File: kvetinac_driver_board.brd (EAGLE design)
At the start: 73.7 x 50.8 mm, 149 parts, among them IC1 MEGA128-A, IC3 74HC238D, IC4 VNH2SP30, IC5 VNH2SP30, J1 PINHD-1X1SMD2.4MM, J10 PINHD-1X1SMD2.4MM, J11 PINHD-1X1SMD2.4MM, J12 PINHD-1X1SMD2.4MM, J13 PINHD-1X1SMD2.4MM, J14 PINHD-1X1SMD2.4MM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

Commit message: AREF pripojen pres 100nF ke GND, misto k AVCC - umoznuje pouzit interni 2.56V referenci
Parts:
- added C23: 100nF/6,3V, rcl_upravena:C0306
- moved R44 0.51 mm to (44.1, 43.1)
- moved R43 0.38 mm to (46.4, 41.9)
- moved C7 0.13 mm to (49.0, 36.1)
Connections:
- new net AREF: C23.1, IC1.62
- net GND: now also C23.2
- net VPP: no longer IC1.62
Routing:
- net GND: track 22.3 -> 26.1 mm, vias 45 -> 47
- net VPP: track 30.0 -> 27.3 mm
- net AREF: track 0.00 -> 1.61 mm, vias 0 -> 1
- net RXD: track 9.33 -> 8.54 mm
- net TXD: track 9.66 -> 10.2 mm

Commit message: Upraven popis soucastek (Led1 az Led4 a kondenzatory C17, C18, C20).
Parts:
- C17, C18, C20: value 4.7uF/6,3V -> 4,7uF/6,3V
- LED: value (none) -> GREEN
- LED1, LED2, LED3, LED4: value (none) -> RED
- renumbered LED_GREEN to LED
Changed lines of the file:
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@@
 <?xml version="1.0" encoding="utf-8"?>
 <!DOCTYPE eagle SYSTEM "eagle.dtd">
-<eagle version="6.2">
+<eagle version="6.1">
 <drawing>
 <settings>
@@
 <element name="R34" library="rcl" package="R0603" value="4k7" x="57.658" y="12.954" rot="R180"/>
 <element name="R35" library="rcl" package="R0603" value="4k7" x="56.642" y="14.605" rot="R180"/>
-<element name="LED_GREEN" library="led" package="CHIPLED_0805" value="" x="39.497" y="33.274" rot="MR90"/>
+<element name="LED" library="led" package="CHIPLED_0805" value="GREEN" x="39.497" y="33.274" rot="MR90"/>
 <element name="R36" library="rcl" package="R0603" value="1k" x="35.941" y="31.623" rot="MR180"/>
 <element name="FERITE_BEAD" library="rcl" package="R0603" value="10uH" x="49.149" y="32.385" rot="MR0"/>
@@
 <element name="STOP_BUTTON" library="pinhead" package="1X02" value="" x="41.529" y="30.226" rot="R90"/>
 <element name="R47" library="rcl" package="R0603" value="220" x="44.323" y="30.598" rot="R270"/>
-<element name="LED1" library="led" package="CHIPLED_0805" value="" x="35.179" y="7.493" rot="MR180"/>
-<element name="LED2" library="led" package="CHIPLED_0805" value="" x="35.179" y="14.986" rot="MR0"/>
-<element name="LED3" library="led" package="CHIPLED_0805" value="" x="35.179" y="34.29" rot="MR180"/>
-<element name="LED4" library="led" package="CHIPLED_0805" value="" x="35.306" y="45.085" rot="MR0"/>
+<element name="LED1" library="led" package="CHIPLED_0805" value="RED" x="35.179" y="7.493" rot="MR180"/>
+<element name="LED2" library="led" package="CHIPLED_0805" value="RED" x="35.179" y="14.986" rot="MR0"/>
+<element name="LED3" library="led" package="CHIPLED_0805" value="RED" x="35.179" y="34.29" rot="MR180"/>
+<element name="LED4" library="led" package="CHIPLED_0805" value="RED" x="35.306" y="45.085" rot="MR0"/>
 <element name="IC3" library="74" package="SO16" value="74HC238D" x="57.785" y="11.049" rot="MR90"/>
 <element name="R49" library="rcl" package="R0603" value="470R" x="64.262" y="6.477" rot="MR90"/>
@@
 <element name="R69" library="rcl" package="R0603" value="220" x="57.15" y="40.767" rot="R90"/>
 <element name="R70" library="rcl" package="R0603" value="220" x="58.7375" y="40.767" rot="R90"/>
-<element name="C17" library="rcl" package="C0805" value="4.7uF/6,3V" x="57.277" y="4.572" rot="MR180"/>
-<element name="C18" library="rcl" package="C0805" value="4.7uF/6,3V" x="54.356" y="13.462" rot="R90"/>
-<element name="C20" library="rcl" package="C0805" value="4.7uF/6,3V" x="42.1798" y="47.9425" rot="MR90"/>
+<element name="C17" library="rcl" package="C0805" value="4,7uF/6,3V" x="57.277" y="4.572" rot="MR180"/>
+<element name="C18" library="rcl" package="C0805" value="4,7uF/6,3V" x="54.356" y="13.462" rot="R90"/>
+<element name="C20" library="rcl" package="C0805" value="4,7uF/6,3V" x="42.1798" y="47.9425" rot="MR90"/>
 <element name="IC4" library="vacha" package="MULTIPOWERSO-30" value="VNH2SP30" x="25.4" y="39.37" rot="R90"/>
 <element name="IC5" library="vacha" package="MULTIPOWERSO-30" value="VNH2SP30" x="25.4" y="11.43" rot="R90"/>
@@
 <contactref element="C1" pad="2"/>
 <contactref element="C2" pad="2"/>
-<contactref element="LED_GREEN" pad="C"/>
+<contactref element="LED" pad="C"/>
 <contactref element="P_SERVA_GND_OUT" pad="7"/>
 <contactref element="P_SERVA_GND_OUT" pad="6"/>
@@
 <signal name="N$21">
 <contactref element="R36" pad="2"/>
-<contactref element="LED_GREEN" pad="A"/>
+<contactref element="LED" pad="A"/>
 <wire x1="38.442" y1="33.274" x2="38.447" y2="33.274" width="0.254" layer="16"/>
 <wire x1="36.791" y1="31.623" x2="38.442" y2="33.274" width="0.254" layer="16"/>

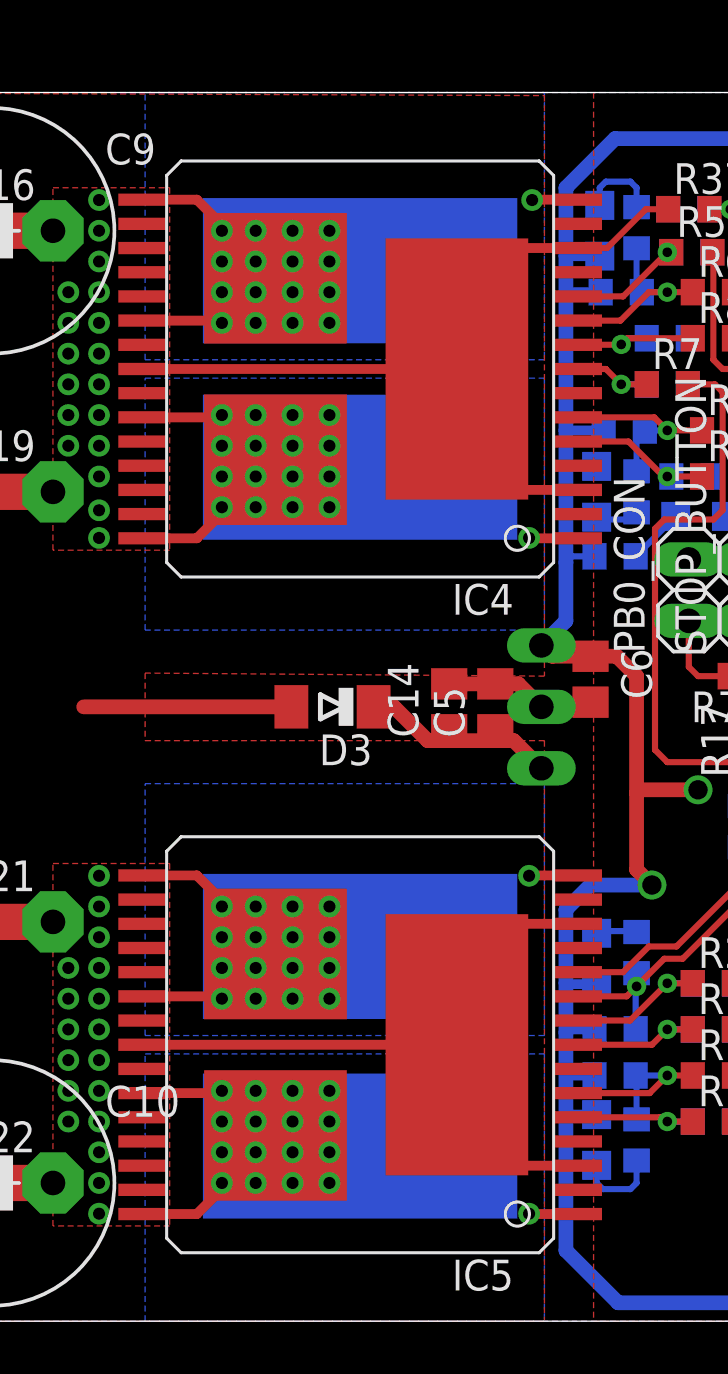
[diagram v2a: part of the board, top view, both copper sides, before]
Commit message: Nov? verze: Upraveny plosky pod drivery VNH2SP30. Pridany vie pod drivery VNH2SP30 - kvuli umozneni pripajeni z druhe strany.
Upraven DESCRIPTION:
Pridany INSTRUKCE PRO VYROBU a pro PRVNI OZIVENI DESKY.
Popsany vsechny veci kolem desky a jeji vyroby.
VSICHNI POVINNE PROCIST!!!
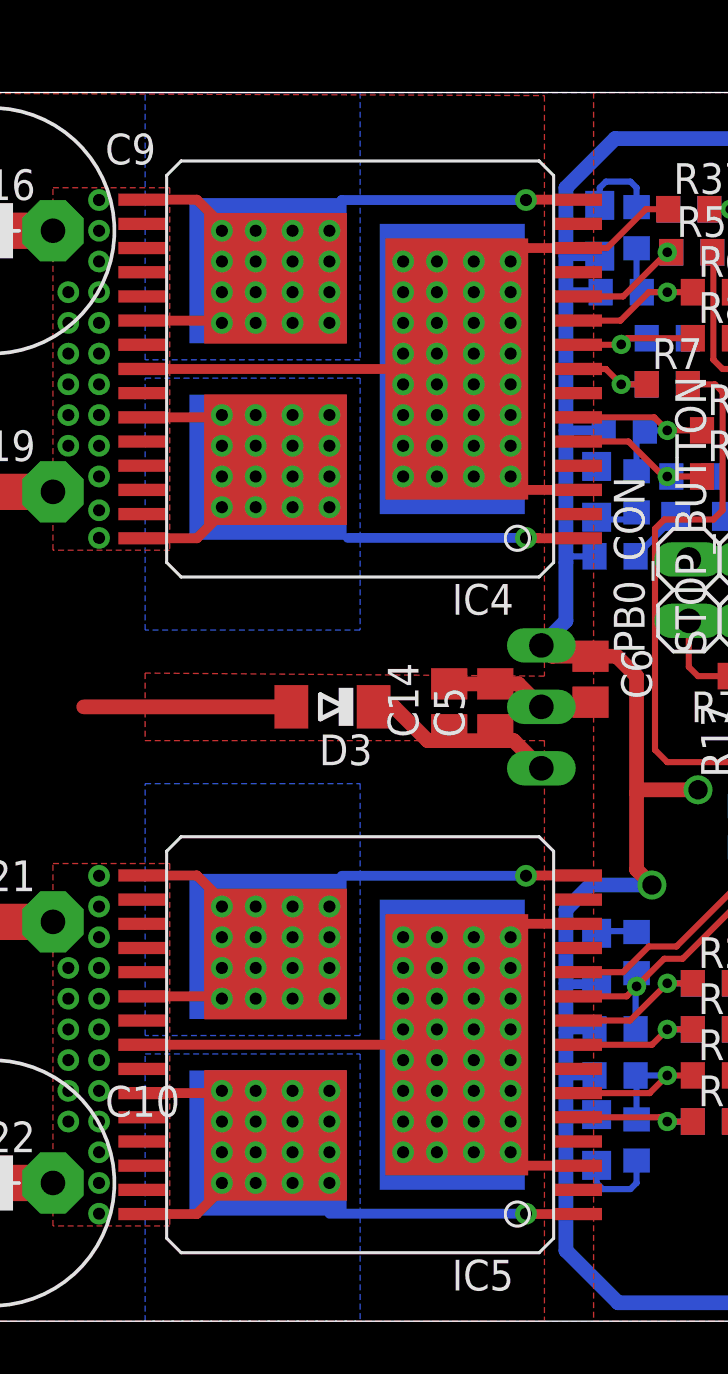
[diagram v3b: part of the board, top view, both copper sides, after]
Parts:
- added VCCA, VCCB: CABEL_SMDCABEL_SMD_12*6MM, cabel_smd:CABEL_SMD_12*6MM
- OUTA_1, OUTA_2, OUTB_1, OUTB_2: value CABEL_SMD -> CABEL_SMDCABEL_SMD_6.5*6MM; device cabel_smd:CABEL_SMD -> cabel_smd:CABEL_SMD_6.5*6MM
- moved OUTA_2 3.81 mm to (21.6, 7.37)
- moved OUTA_1 3.81 mm to (21.6, 35.3)
- moved OUTB_1 3.81 mm to (21.6, 43.4)
- moved OUTB_2 3.81 mm to (21.6, 15.5)
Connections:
- net VCC: now also VCCA.P$1, VCCB.P$1
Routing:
- net OUTA_2: track 15.2 -> 23.5 mm
- net OUTB_1: track 16.3 -> 24.3 mm
- net OUTB_2: track 15.2 -> 23.0 mm
- net OUTA_1: track 15.6 -> 23.1 mm
- net VCC: vias 0 -> 64
